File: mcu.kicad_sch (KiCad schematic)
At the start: 5 parts, among them J3 USB_C_Receptacle_USB2.0_16P, M1 Module-stlink-0.1, M3 Module-mega-mcu144-0.6

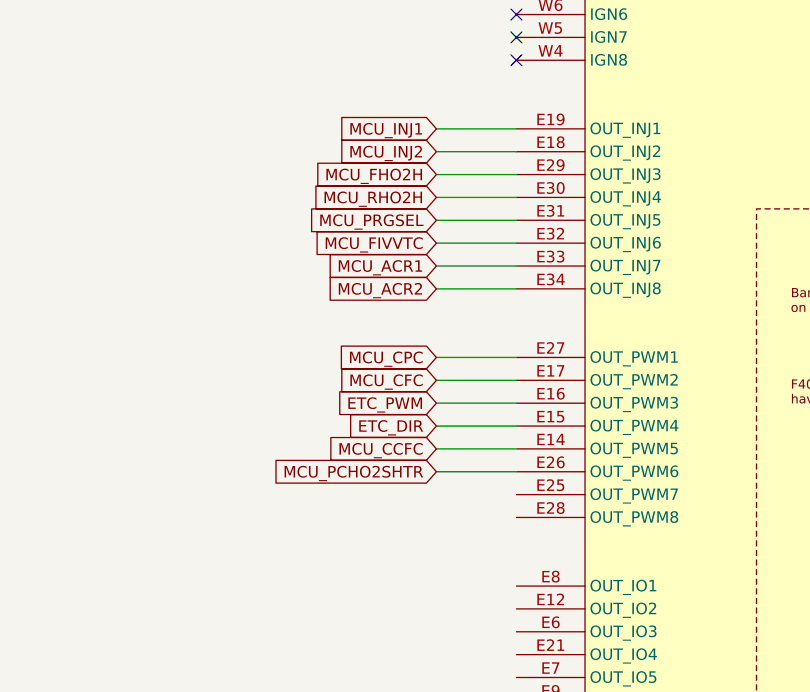
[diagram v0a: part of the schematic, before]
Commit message: pwm for heaters, minor routing and via changes, teardrops
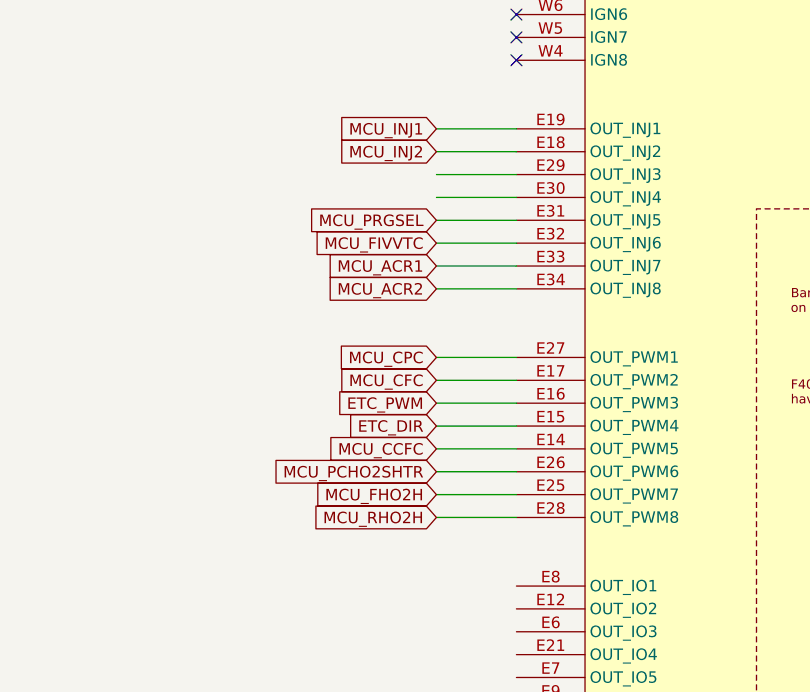
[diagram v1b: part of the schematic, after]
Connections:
- net MCU_FHO2H: now also M3.E25 (OUT_PWM7); no longer M3.E29 (OUT_INJ3)
- net MCU_RHO2H: now also M3.E28 (OUT_PWM8); no longer M3.E30 (OUT_INJ4)

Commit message: some documentation and etc_dir added
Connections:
- net ETC_DIS: now reaches M3.E2 (SPI2_MISO)
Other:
- note added: "TODO: Does this work here?"
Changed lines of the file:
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@@
+	(wire
+		(pts
+			(xy 231.14 27.94) (xy 248.92 27.94)
+		)
+		(stroke
+			(width 0)
+			(type default)
+		)
+	)
 	(wire
 		(pts
@@
 		)
 	)
+	(text "TODO: Does this work here?"
+		(exclude_from_sim no)
+		(at 257.048 25.146 0)
+		(effects
+			(font
+				(size 1.27 1.27)
+			)
+		)
+	)
 	(text "TODO: Do we really need post CAT?"
 		(exclude_from_sim no)
@@
 				(hide yes)
 			)
+		)
+	)
+	(global_label "ETC_DIS"
+		(shape input)
+		(at 248.92 27.94 0)
+		(fields_autoplaced yes)
+		(effects
+			(font
+				(size 1.27 1.27)
+			)
+			(justify left)
+		)
+		(property "Intersheetrefs" "${INTERSHEET_REFS}"
+			(at 259.3437 27.94 0)
+			(effects
+				(font
+					(size 1.27 1.27)
+				)
+				(justify left)
+				(hide yes)
+			)
